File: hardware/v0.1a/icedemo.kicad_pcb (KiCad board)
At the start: 4 copper layers, 80 x 40 mm, 54 parts, among them J1 SNES, J2 HDMI_A, SW1 TACT, U1 74LVC2T45, U2 74LVC2T45, U3 74LVC2T45, U4 SII902xA-mod, U5 TLV62568DBV

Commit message: First routing pass.
State after Electronics Let's Play stream.
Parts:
- moved SW1 32.1 mm to (52.6, 35.5), turned to 180 degrees
- moved R12 9.17 mm to (83.2, 37.5)
- moved R14 8.35 mm to (91.2, 58.0), turned to 90 degrees
- moved R15 8.16 mm to (92.1, 58.0), turned to 90 degrees
- moved R11 7.40 mm to (83.2, 36.6)
- moved R2 6.36 mm to (48.4, 38.6), turned to 90 degrees
- moved R3 6.22 mm to (48.4, 45.7), turned to 90 degrees
- moved R16 5.35 mm to (93.9, 58.0), turned to -90 degrees
- moved C6 5.00 mm to (48.3, 42.6), turned to -90 degrees
- moved U2 4.76 mm to (48.9, 40.6), turned to 180 degrees
- moved C5 4.53 mm to (48.2, 59.3), turned to -90 degrees
- moved L1 4.15 mm to (88.2, 39.0)
- moved L4 3.47 mm to (95.8, 45.4)
- moved C2 3.44 mm to (49.4, 42.6), turned to -90 degrees
- moved C23 3.42 mm to (96.1, 46.5)
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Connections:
- A1 pad 10: /DE -> /IDCK
- A1 pad 11: /VSYNC -> /VD8
- A1 pad 12: /HSYNC -> /VD9
- A1 pad 13: /IDCK -> /VD10
- A1 pad 14: /VD0 -> /VD11
- A1 pad 15: /VD1 -> /CSCL
- A1 pad 16: /VD2 -> /CSDA
- A1 pad 17: /VD3 -> /GPSEL
- A1 pad 18: /VD4 -> /GPDAT1
- A1 pad 19: /VD5 -> /GPDAT0
- A1 pad 2: /GPCLK -> /VD0
- A1 pad 20: /VD6 -> /GPLATCH
- A1 pad 21: /VD7 -> /GPCLK
- A1 pad 22: /VD8 -> /DE
- A1 pad 23: /VD9 -> /VSYNC
- A1 pad 24: /VD10 -> /HSYNC
- A1 pad 25: /VD11 -> /SPDIF
- A1 pad 3: /GPLATCH -> /VD1
- A1 pad 4: /GPDAT0 -> /VD2
- A1 pad 5: /GPDAT1 -> /VD3
- A1 pad 6: /GPSEL -> /VD4
- A1 pad 7: /CSDA -> /VD5
- A1 pad 8: /CSCL -> /VD6
- A1 pad 9: /SPDIF -> /VD7
- U4 pad 73: (no net) -> GND
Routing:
- net /CDONE/~{RST}: track 0.00 -> 48.9 mm, vias 0 -> 2
- net /CSCL: track 0.00 -> 42.8 mm, vias 0 -> 1
- net /CVCC12: track 4.00 -> 45.5 mm, vias 1 -> 6
- net /CSDA: track 0.00 -> 39.6 mm, vias 0 -> 1
- net /IOVCC: track 3.52 -> 37.4 mm, vias 0 -> 4
- net +1V2: track 0.00 -> 27.2 mm
- net /SPDIF: track 0.00 -> 23.6 mm, vias 0 -> 1
- net /HSYNC: track 0.00 -> 22.8 mm, vias 0 -> 1
- net /DE: track 0.00 -> 22.4 mm, vias 0 -> 1
- net /VSYNC: track 0.00 -> 22.3 mm, vias 0 -> 1
- net /VD0: track 0.00 -> 16.4 mm
- net /CEC: track 0.00 -> 16.1 mm, vias 0 -> 2
- net Net-(A1-Pad31): track 0.00 -> 15.1 mm
- net /GPLATCH: track 0.00 -> 14.9 mm
- net /VD1: track 0.00 -> 14.3 mm
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- added copper zone on In2.Cu, net +3V3
- added copper zone on In2.Cu, net +5V
- added copper zone on B.Cu, net GND
- added copper zone on F.Cu, net GND
- added copper zone on In1.Cu, net GND
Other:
- board text added: "V0.1a"
- board text added: "iCEBitsy Demo Board"

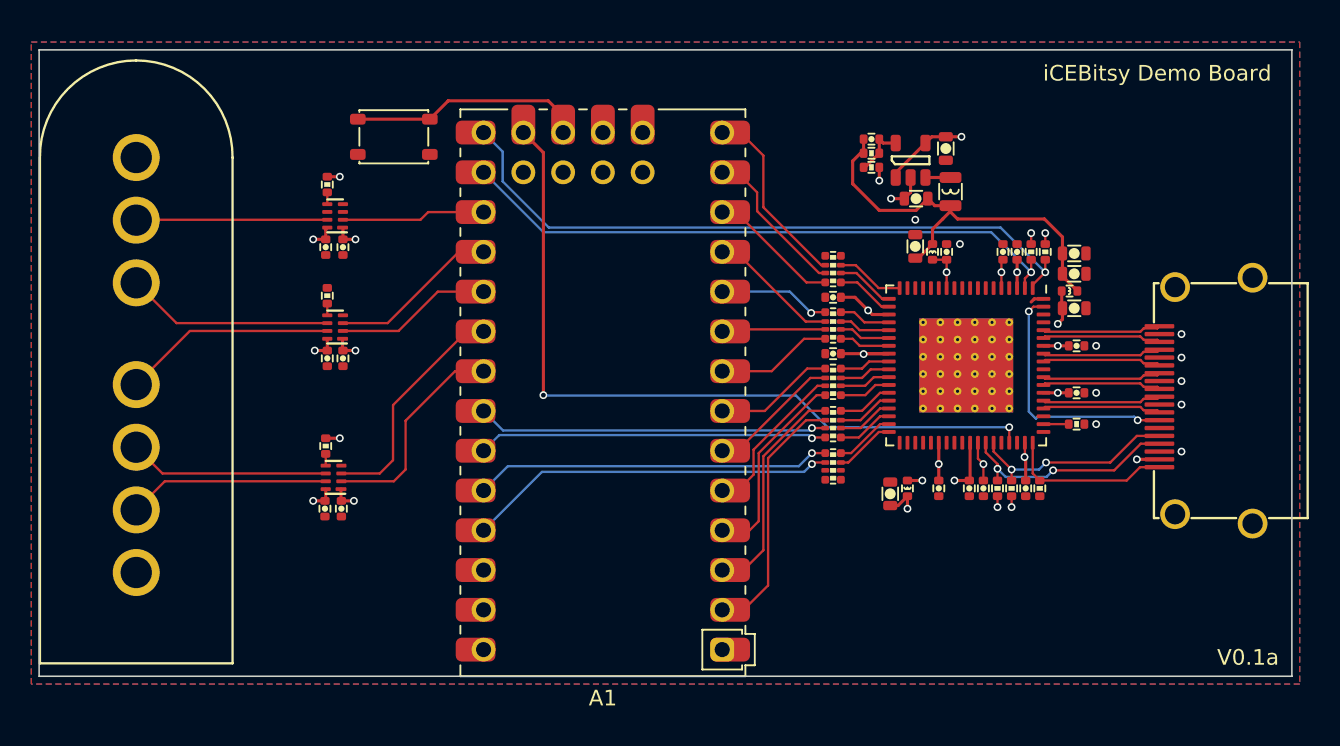
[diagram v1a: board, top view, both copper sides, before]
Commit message: Improved layout from Aug 10th stream.
Added GPIO expander and AUX connector.
Compressed board a bit.
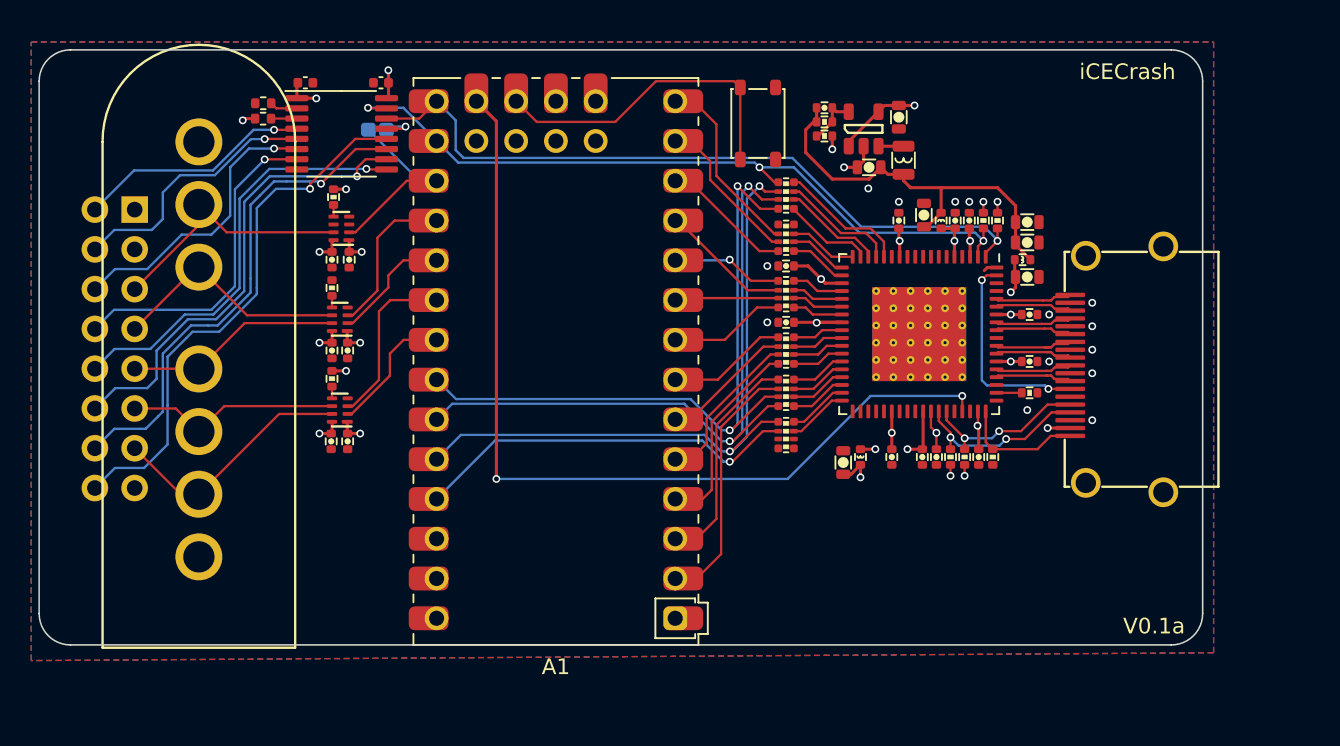
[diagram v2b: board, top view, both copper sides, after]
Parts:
- added C26: 100n, Capacitor_SMD:C_0402_1005Metric, F.Cu at (47.0, 32.1)
- added C27: 100n, Capacitor_SMD:C_0402_1005Metric, F.Cu at (51.8, 32.1)
- added J3: pkl_jumper, pkl_jumpers:J_0603, B.Cu at (51.6, 35.1)
- added J5: Conn_02x08_Odd_Even, Connector_PinHeader_2.54mm:PinHeader_2x08_P2.54mm_Horizontal, B.Cu at (36.1, 40.2)
- added R17: 33R, pkl_dipol:R_Array_Convex_4x0402, F.Cu at (77.7, 39.3)
- added R18: 10k, Resistor_SMD:R_0402_1005Metric, F.Cu at (44.3, 34.4)
- added R19: 10k, Resistor_SMD:R_0402_1005Metric, F.Cu at (44.3, 33.4)
- added U6: PCA6408APW, Package_SO:TSSOP-16_4.4x5mm_P0.65mm, F.Cu at (49.3, 35.4)
- moved SW1 23.3 mm to (75.9, 34.7), turned to -90 degrees
- moved J2 6.04 mm to (96.8, 50.4)
- moved C1 4.32 mm to (49.7, 55.0)
- moved R1 4.32 mm to (48.7, 51.0)
- moved U1 4.32 mm to (49.2, 53.0)
- moved C5 4.32 mm to (48.6, 55.0)
- moved J1 4.12 mm to (40.2, 62.4)
- moved C14 3.65 mm to (84.9, 40.9)
- moved C15 3.65 mm to (88.5, 40.9)
- moved C19 3.65 mm to (89.4, 40.9)
- moved R8 3.65 mm to (90.3, 40.9)
- moved R9 3.65 mm to (91.2, 40.9)
- moved A1 3.61 mm to (63.0, 49.9)
- moved C10 3.61 mm to (90.0, 56.0)
- moved C11 3.61 mm to (87.3, 56.0)
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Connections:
- U4 pad 14: unconnected-(U4-Pad14) -> Net-(R17-Pad2)
- U4 pad 15: unconnected-(U4-Pad15) -> Net-(R17-Pad4)
- U4 pad 16: unconnected-(U4-Pad16) -> Net-(R17-Pad6)
- U4 pad 17: unconnected-(U4-Pad17) -> Net-(R17-Pad8)
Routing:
- net /G7: track 0.00 -> 34.5 mm, vias 0 -> 1
- net /G6: track 0.00 -> 32.1 mm, vias 0 -> 1
- net /G5: track 0.00 -> 29.9 mm, vias 0 -> 1
- net /G4: track 0.00 -> 27.3 mm, vias 0 -> 1
- net /G3: track 0.00 -> 21.0 mm, vias 0 -> 1
- net /VSYNC: track 22.3 -> 43.3 mm, vias 1 -> 2
- net /DE: track 22.4 -> 43.1 mm, vias 1 -> 2
- net /HSYNC: track 22.8 -> 42.8 mm, vias 1 -> 2
- net /G2: track 0.00 -> 18.4 mm, vias 0 -> 1
- net /G1: track 0.00 -> 16.8 mm, vias 0 -> 1
- net /G0: track 0.00 -> 15.0 mm, vias 0 -> 1
- net +3V3: track 9.93 -> 20.2 mm, vias 8 -> 10
- net /CDONE/~{RST}: track 48.9 -> 57.6 mm
- net Net-(R17-Pad2): track 0.00 -> 8.29 mm
- net /CSDA: track 39.6 -> 47.6 mm, vias 1 -> 3
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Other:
- board size 80 x 40 mm -> 74.3 x 38 mm
- board text added: "iCECrash"
- board text removed: "iCEBitsy Demo Board"
